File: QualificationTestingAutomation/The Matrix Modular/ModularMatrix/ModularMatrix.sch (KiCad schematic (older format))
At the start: 0 parts

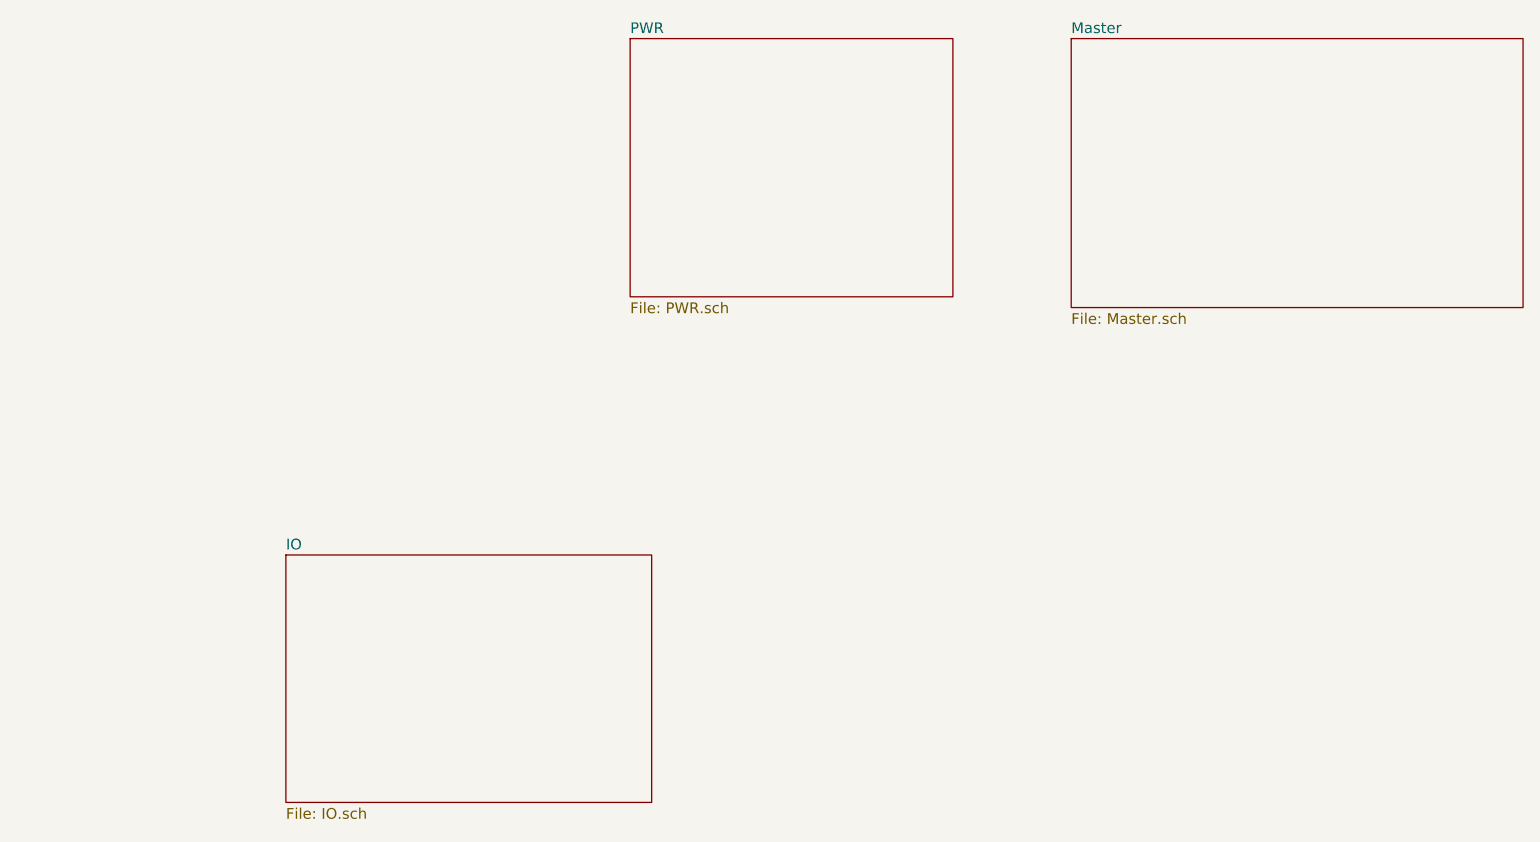
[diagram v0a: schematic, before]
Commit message: Schematic Clean ups the layout needs to be changed
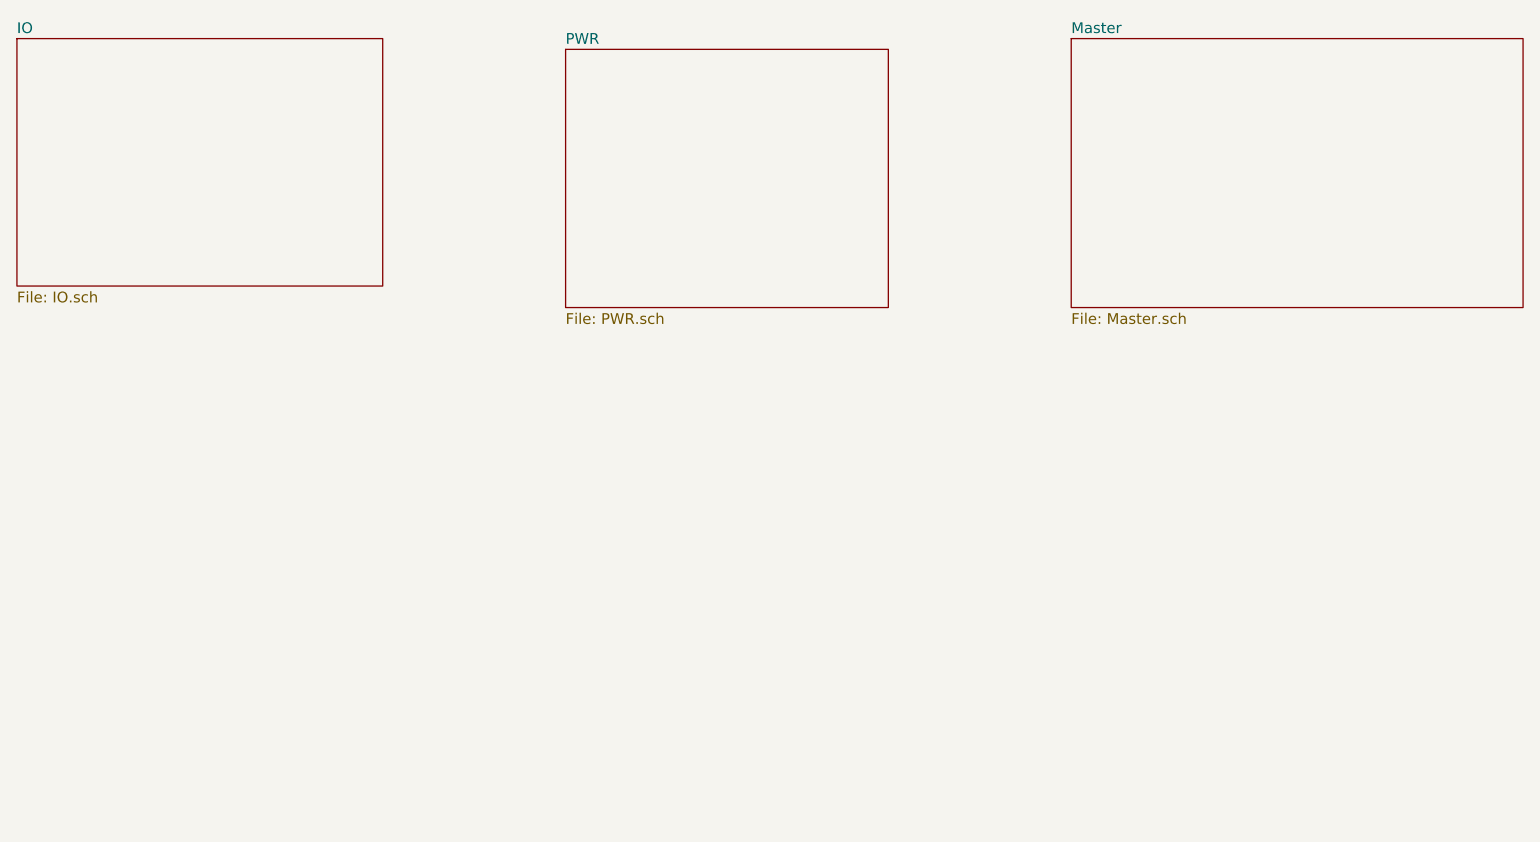
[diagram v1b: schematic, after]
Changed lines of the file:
@@
 EESchema Schematic File Version 4
 LIBS:ModularMatrix-cache
-EELAYER 26 0
+EELAYER 29 0
 EELAYER END
 $Descr A4 11693 8268
@@
 $EndSheet
 $Sheet
-S 6050 900  1500 1200
+S 5750 950  1500 1200
 U 5D94288A
 F0 "PWR" 50
@@
 $EndSheet
 $Sheet
-S 4450 3300 1700 1150
+S 3200 900  1700 1150
 U 5D968A33
 F0 "IO" 50
